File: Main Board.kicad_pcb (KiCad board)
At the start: 2 copper layers, 371 parts, among them J1 Motor Y, J10 CA58SUB-B, J11 PC6 EPSON MAINBOARD, J12 Y AXIS, J13 Z AXIS, J14 LED 1, J15 LED 2, J16 Power Input, J17 VS, J18 12V, J19 5V, J2 Motor Z, J20 3.3V, J21 TABLE SENSOR, J22 INPUT1, J23 INPUT2, J24 PHOTO SENSOR EMITER, J25 PHOTO SENSOR RECEIVER, J26 ANALOG, J27 INPUT3, J28 OUT1, J29 OUT2, J3 USB_B, J30 RELAY, J31 EMERGENCY, J32 EPSON POWER IN, J33 EPSON BOARD POWER, J34 Display, J35 SPI Interface, J36 I2C Interface, J37 LED4, J38 LED3, J39 Key 3, J4 SWD, J40 Key 4, J41 Key 1, J42 Key 2, J5 DEBUG, J6 LIMIT Y BACK, J7 LIMIT Y FRONT, J8 LIMIT Z UP, J9 LIMIT Z DOWN, K1 S13-24V-2C, Q1 2N7002K, Q10 2N7002K, Q11 BC817, Q12 BC817, Q13 BC817, Q14 2N7002K, Q15 2N7002K, Q16 2N7002K, Q17 BC817, Q18 2N7002K, Q19 2N7002K, Q2 2N7002K, Q20 2N7002K, Q21 2N7002K, Q3 2N7002K, Q4 2N7002K, Q5 2N7002K, Q6 2N7002K, Q7 2N7002K, Q8 YJS9435A, Q9 2N7002K, U1 TMC2209-LA, U10 74HC2G32, U11 74HC245, U12 SHTC3, U2 TMC2209-LA, U3 STM32F401VETx, U4 USBUF02W6, U5 74HC245, U6 MCP16301, U7 A4403, U8 MCP16301, U9 MCP6002-xSN, Y1 8MHz

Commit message: Routing of the power supplies are finished
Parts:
- removed the D11 at (93.3, -11.9)
- removed D46, D47, D48: SKL32, Diode_SMD:D_SOD-123F
- removed D49, D50: SD05C.TCT, Diode_SMD:D_SOD-323
- removed the FB1 at (46.9, -7.78)
- removed FB10, FB11: 1000@100MHz, Inductor_SMD:L_0805_2012Metric
- removed FB9: 60Ohm@100MHz, Inductor_SMD:L_0805_2012Metric
- removed the J12 at (83.8, -47.5)
- removed the R12 at (116.4, -77.0)
- removed the R16 at (121.7, -57.5)
- removed the TP11 at (65.0, -72.1)
- removed the U2 at (112.9, -24.8)
- added C79: 1nF, Capacitor_SMD:C_0603_1608Metric, F.Cu at (266.3, 26.7)
- added D23: 1N4448WS-7-F, Diode_SMD:D_SOD-323, F.Cu at (92.5, 44.0)
- added H4: MH, MountingHole:MountingHole_3.5mm_Pad_Via, F.Cu at (121.0, 104.0)
- added Q10: 2N7002K, Package_TO_SOT_SMD:SOT-23, F.Cu at (50.5, -53.2)
- added Q7: 2N7002K, Package_TO_SOT_SMD:SOT-23, F.Cu at (103.2, -51.6)
- added R114: 100Ω, Resistor_SMD:R_0603_1608Metric, F.Cu at (165.4, -34.8)
- added R115: 47kΩ, Resistor_SMD:R_0603_1608Metric, F.Cu at (161.2, -33.7)
- added R116: 47kΩ, Resistor_SMD:R_0603_1608Metric, F.Cu at (165.4, -37.3)
- added R97: 20Ω, Resistor_SMD:R_0603_1608Metric, F.Cu at (253.0, 38.0)
- added TP1: Z_OB2, TestPoint:TestPoint_Pad_D1.5mm, F.Cu at (259.1, 66.9)
- D1, D10, D12, D2, D3, D4, D5, D6, D7, D8, D9: value SK25 -> SMAJ26CA; footprint Diode_SMD:D_SMB -> Diode_SMD:D_SMA
- D11: renamed from C79; value 1nF -> SMAJ26CA; footprint Capacitor_SMD:C_0603_1608Metric -> Diode_SMD:D_SMA
- D13, D16: value SK25 -> OF-SMD2012G-1; footprint Diode_SMD:D_SMB -> Diode_SMD:D_0805_2012Metric
- D14, D15: value SK25 -> SD05C.TCT; footprint Diode_SMD:D_SMB -> Diode_SMD:D_SOD-323
- D18, D39: value SD05C.TCT -> SMAJ26CA; footprint Diode_SMD:D_SOD-323 -> Diode_SMD:D_SMA
- D19: value SD05C.TCT -> OF-SMD2012G-1; footprint Diode_SMD:D_SOD-323 -> Diode_SMD:D_0805_2012Metric
- D20: value OF-SMD2012G-1 -> MMSZ5240B-7-F; footprint Diode_SMD:D_0805_2012Metric -> Diode_SMD:D_SOD-123
- D22: value P4SMA30CA -> B140-13-F
- D24: value MMSZ5240B-7-F -> MMSZ5236BS-7-F; footprint Diode_SMD:D_SOD-123 -> Diode_SMD:D_SOD-323
- D25: value OF-SMD2012G-1 -> B140-13-F; footprint Diode_SMD:D_0805_2012Metric -> Diode_SMD:D_SMA
- D26: value B140-13-F -> SK35SMA
- D28: value MMSZ5236BS-7-F -> 1N4448WS-7-F
- D29: value B140-13-F -> 1N4448WS-7-F; footprint Diode_SMD:D_SMA -> Diode_SMD:D_SOD-323
- D30: value SK35SMA -> 1N4448WS-7-F; footprint Diode_SMD:D_SMA -> Diode_SMD:D_SOD-323
- D35, D36: value 1N4448WS-7-F -> SD05C.TCT
- D37: renamed from D23; value OF-SMD2012G-1 -> SD05C.TCT; footprint Diode_SMD:D_0805_2012Metric -> Diode_SMD:D_SOD-323
- D38: value 1N4448WS-7-F -> SMAJ26CA; footprint Diode_SMD:D_SOD-323 -> Diode_SMD:D_SMA
- D40, D41: value SD05C.TCT -> SKL32; footprint Diode_SMD:D_SOD-323 -> Diode_SMD:D_SOD-123F
- D42, D43: value B130-13-F -> SKL32; footprint Diode_SMD:D_SMA -> Diode_SMD:D_SOD-123F
- D44: value B130-13-F -> SD05C.TCT; footprint Diode_SMD:D_SMA -> Diode_SMD:D_SOD-323
- D45: value SKL32 -> SD05C.TCT; footprint Diode_SMD:D_SOD-123F -> Diode_SMD:D_SOD-323
- F2, F3: value SN010-60 -> 0ZCJ0050AF2E
- F4: value SR050 -> 0ZCK0100FF2E
- FB1: renamed from D37; value 1N4448WS-7-F -> 60Ohm@100MHz; footprint Diode_SMD:D_SOD-323 -> Inductor_SMD:L_0805_2012Metric
- J12: renamed from H4; value MH -> Y AXIS; footprint MountingHole:MountingHole_3.5mm_Pad_Via -> Connector_JST:JST_PH_B3B-PH-K_1x03_P2.00mm_Vertical
- R1: value 1kΩ -> 0Ω
- R10: value 10kΩ -> 47Ω
- R100, R101, R17: value 4.7kΩ -> 330Ω
- R103, R104, R105: value 1kΩ -> 4.7kΩ
- R107, R109: value 2.2kΩ -> 1kΩ
- R108, R31: value 0Ω -> 1kΩ
- R110: value 100Ω -> 2.2kΩ
- R111: value 100Ω -> 0Ω
- R112: value 47kΩ -> 2.2kΩ
- R113, R23, R24, R25: value 47kΩ -> 100Ω
- R12: renamed from Q7; value 2N7002K -> 10kΩ; footprint Package_TO_SOT_SMD:SOT-23 -> Resistor_SMD:R_0603_1608Metric
- R13: value 330Ω -> 0Ω
- R15: value 4.7kΩ -> 0Ω
- R16: renamed from Q10; value 2N7002K -> 0Ω; footprint Package_TO_SOT_SMD:SOT-23 -> Resistor_SMD:R_0603_1608Metric
- R19, R20, R21, R62: value 100Ω -> 4.7kΩ
- R2, R6: value 100kΩ -> 1kΩ
- R27, R84: value 100Ω -> 47kΩ
- R28, R40: value 1kΩ -> 47kΩ
- R29: value 0Ω -> 47kΩ
- R3, R7: value 100mΩ -> 100kΩ; footprint Resistor_SMD:R_2010_5025Metric -> Resistor_SMD:R_0603_1608Metric
- R30: value 0Ω -> 100Ω
- R32: value NI -> 0Ω
- R35: value 100Ω -> NI
- R36: value 100kΩ -> 0Ω
- R37: value 47kΩ -> 0Ω
- R39: value 1kΩ -> 100kΩ
- R41: value 1kΩ -> 100Ω
- R42: value 10kΩ -> 1kΩ; footprint Resistor_SMD:R_0805_2012Metric -> Resistor_SMD:R_0603_1608Metric
- R43: value 330Ω -> 1kΩ
- R45: value 100kΩ -> 10kΩ; footprint Resistor_SMD:R_0603_1608Metric -> Resistor_SMD:R_0805_2012Metric
- R46: value 2.7kΩ -> 330Ω
- R47: value 140kΩ -> 1kΩ
- R48: value 10kΩ -> 100kΩ
- R49: value 100kΩ -> 2.7kΩ
- R5: value 1kΩ -> 100mΩ; footprint Resistor_SMD:R_0603_1608Metric -> Resistor_SMD:R_2010_5025Metric
- R50: value 47Ω -> 140kΩ
- R51: value 100mΩ -> 10kΩ; footprint Resistor_SMD:R_1206_3216Metric -> Resistor_SMD:R_0603_1608Metric
- R52: value 100mΩ -> 100kΩ; footprint Resistor_SMD:R_1206_3216Metric -> Resistor_SMD:R_0603_1608Metric
- R53: value 31.2kΩ -> 47Ω
- R54: value 10kΩ -> 100mΩ; footprint Resistor_SMD:R_0603_1608Metric -> Resistor_SMD:R_1206_3216Metric
- R55: value 3.92kΩ -> 100mΩ; footprint Resistor_SMD:R_0603_1608Metric -> Resistor_SMD:R_1206_3216Metric
- R56: value 750Ω -> 31.2kΩ
- R58: value 4.7kΩ -> 3.92kΩ
- R59: value 4.7kΩ -> 750Ω
- R61: value 100kΩ -> 4.7kΩ
- R63: value 100Ω -> 10kΩ
- R65, R66: value 100kΩ -> 100Ω
- R67, R68, R69: value 47kΩ -> 100kΩ
- R71, R72, R73: value NI -> 47kΩ
- R77: value 10kΩ -> NI
- R79: value 100kΩ -> NI
- R80: value 100kΩ -> 10kΩ
- R81: value 47kΩ -> NI
- R82, R83, R95: value 100Ω -> 100kΩ
- R85: value 0Ω -> 100Ω; footprint Resistor_SMD:R_0805_2012Metric -> Resistor_SMD:R_0603_1608Metric
- R86, R87: value NI -> 100Ω; footprint Resistor_SMD:R_0805_2012Metric -> Resistor_SMD:R_0603_1608Metric
- R88: value 100kΩ -> 0Ω; footprint Resistor_SMD:R_0603_1608Metric -> Resistor_SMD:R_0805_2012Metric
- R89: value 100kΩ -> NI; footprint Resistor_SMD:R_0603_1608Metric -> Resistor_SMD:R_0805_2012Metric
- R9: value 47RΩ -> 100mΩ; footprint Resistor_SMD:R_0603_1608Metric -> Resistor_SMD:R_2010_5025Metric
- R90: value 1kΩ -> NI; footprint Resistor_SMD:R_0603_1608Metric -> Resistor_SMD:R_0805_2012Metric
- R93: value 20Ω -> 1kΩ
- R94: value 20Ω -> 100kΩ
- R96: value 100Ω -> 20Ω
- R98: value 330Ω -> 100Ω
- R99: value 4.7kΩ -> 100Ω
- TP11: renamed from R97; value 330Ω -> 3.3V; footprint Resistor_SMD:R_0603_1608Metric -> TestPoint:TestPoint_Pad_D1.5mm
- U2: renamed from TP1; value Z_OB2 -> TMC2209-LA; footprint TestPoint:TestPoint_Pad_D1.5mm -> footprints:TMC2209-LA
- moved R3 224.9 mm to (253.9, 69.4)
- moved FB3 224.4 mm to (255.1, 64.1)
- moved FB2 223.7 mm to (263.0, 53.9)
- moved D3 223.4 mm to (249.5, 54.7)
- moved C9 222.4 mm to (263.3, 59.2)
- moved C6 221.9 mm to (262.8, 56.6)
- moved FB1 219.6 mm to (241.3, 71.8)
- moved D2 218.1 mm to (241.5, 59.3)
- moved FB4 217.4 mm to (245.7, 70.2)
- moved C4 216.9 mm to (259.3, 61.0)
- moved C1 216.7 mm to (226.5, 66.0)
- moved J1 216.7 mm to (226.5, 55.8)
- moved U1 216.5 mm to (257.2, 56.1)
- moved D1 216.3 mm to (227.0, 74.1)
- moved D5 215.4 mm to (241.5, 54.7)
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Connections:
- D1 pad 1: VS -> Net-(C12-Pad1)
- D1 pad 2: Net-(C12-Pad1) -> GND
- D10 pad 1: Net-(C26-Pad1) -> Net-(C25-Pad2)
- D11 pad 1: KEY_3 -> Net-(C27-Pad2)
- D11 pad 2: GND -> Net-(C25-Pad2)
- D12 pad 1: Net-(C28-Pad1) -> Net-(C26-Pad1)
- D12 pad 2: GND -> Net-(C28-Pad1)
- D13 pad 1: VS -> /Microcontroller/LED_STATUS
- D13 pad 2: Net-(C27-Pad2) -> Net-(D13-Pad2)
- D14 pad 1: Net-(C27-Pad2) -> /Sockets/OPE
- D15 pad 1: VS -> /Sockets/OPC1
- D15 pad 2: Net-(C25-Pad2) -> GND
- D16 pad 1: Net-(C25-Pad2) -> GND
- D16 pad 2: GND -> Net-(D16-Pad2)
- D17 pad 1: /Microcontroller/LED_STATUS -> GND
- D18 pad 1: /Sockets/OPE -> GND
- D18 pad 2: GND -> Net-(D18-Pad2)
- D19 pad 1: /Sockets/OPC1 -> GND
- D19 pad 2: GND -> Net-(D19-Pad2)
- D2 pad 1: Net-(C12-Pad1) -> Net-(C14-Pad1)
- D20 pad 1: GND -> VS
- D22 pad 1: GND -> Net-(C51-Pad2)
- D22 pad 2: Net-(D22-Pad2) -> GND
- D24 pad 1: VS -> +12V
- D24 pad 2: Net-(D24-Pad2) -> Net-(D23-Pad2)
- D25 pad 1: GND -> Net-(C61-Pad2)
- D25 pad 2: Net-(D25-Pad2) -> GND
- D26 pad 1: Net-(C51-Pad2) -> Net-(C59-Pad2)
- D26 pad 2: GND -> Net-(D26-Pad2)
- D27 pad 1: Net-(C51-Pad1) -> Net-(C61-Pad1)
- D27 pad 2: Net-(D27-Pad2) -> +3V3
- D28 pad 1: +12V -> Net-(D28-Pad1)
- D28 pad 2: Net-(D27-Pad2) -> GND
- D29 pad 1: Net-(C61-Pad2) -> Net-(D29-Pad1)
- D3 pad 1: VS -> Net-(C13-Pad2)
- D3 pad 2: Net-(C14-Pad1) -> GND
- D30 pad 1: Net-(C59-Pad2) -> VDDA
- D30 pad 2: Net-(D30-Pad2) -> Net-(C73-Pad1)
- D31 pad 1: Net-(C61-Pad1) -> Net-(C73-Pad1)
- D31 pad 2: +3V3 -> GND
- D32 pad 1: Net-(D32-Pad1) -> VDDA
- D32 pad 2: GND -> Net-(C74-Pad1)
- D33 pad 1: Net-(D33-Pad1) -> Net-(C74-Pad1)
- D34 pad 1: VDDA -> Net-(D34-Pad1)
- D34 pad 2: Net-(C73-Pad1) -> GND
- D35 pad 1: Net-(C73-Pad1) -> Net-(D35-Pad1)
- D36 pad 1: VDDA -> Net-(D36-Pad1)
- D36 pad 2: Net-(C74-Pad1) -> GND
- D37 pad 1: GND -> Net-(D37-Pad1)
- D37 pad 2: Net-(D23-Pad2) -> GND
- D38 pad 1: Net-(D38-Pad1) -> 12V_PROTECTED
- D39 pad 1: Net-(D39-Pad1) -> GND
- D39 pad 2: GND -> Net-(D39-Pad2)
- D4 pad 1: Net-(C14-Pad1) -> Net-(C11-Pad2)
- D40 pad 1: Net-(D40-Pad1) -> +3V3
- D40 pad 2: GND -> I2C_SCL
- D41 pad 1: Net-(D41-Pad1) -> I2C_SCL
- D42 pad 1: 12V_PROTECTED -> +3V3
- D42 pad 2: GND -> I2C_SDA
- D43 pad 1: Net-(D43-Pad1) -> I2C_SDA
- D44 pad 1: VS -> Net-(D44-Pad1)
- D44 pad 2: Net-(D43-Pad1) -> GND
- D45 pad 1: +3V3 -> Net-(D45-Pad1)
- D45 pad 2: I2C_SCL -> GND
- D5 pad 1: VS -> Net-(C13-Pad2)
- D5 pad 2: Net-(C13-Pad2) -> Net-(C11-Pad2)
- D6 pad 1: Net-(C13-Pad2) -> Net-(C12-Pad1)
- D6 pad 2: GND -> Net-(C14-Pad1)
- D7 pad 1: VS -> Net-(C26-Pad1)
- D7 pad 2: Net-(C11-Pad2) -> GND
- D8 pad 1: Net-(C11-Pad2) -> Net-(C28-Pad1)
- D9 pad 1: VS -> Net-(C27-Pad2)
- D9 pad 2: Net-(C26-Pad1) -> GND
- F1 pad 1: Net-(D22-Pad2) -> Net-(D18-Pad2)
- FB1 pad 1: Net-(C74-Pad1) -> Net-(C11-Pad2)
- FB1 pad 2: GND -> Net-(FB1-Pad2)
- FB2 pad 1: Net-(C11-Pad2) -> Net-(C13-Pad2)
- FB3 pad 1: Net-(C13-Pad2) -> Net-(C14-Pad1)
- FB4 pad 1: Net-(C14-Pad1) -> Net-(C12-Pad1)
- FB5 pad 1: Net-(C12-Pad1) -> Net-(C25-Pad2)
- FB6 pad 1: Net-(C25-Pad2) -> Net-(C27-Pad2)
- FB7 pad 1: Net-(C27-Pad2) -> Net-(C28-Pad1)
- FB8 pad 1: Net-(C28-Pad1) -> Net-(C26-Pad1)
- J12 pad 1: Net-(H4-Pad1) -> /Sockets/YSTEP
- J28 pad 2: Net-(D39-Pad1) -> Net-(D35-Pad1)
- J29 pad 2: Net-(D40-Pad1) -> Net-(D36-Pad1)
- J30 pad 1: Net-(D41-Pad1) -> Net-(D37-Pad1)
- J31 pad 2: Net-(D43-Pad1) -> Net-(D39-Pad2)
- J37 pad 2: Net-(D49-Pad1) -> Net-(D44-Pad1)
- J38 pad 2: Net-(D50-Pad1) -> Net-(D45-Pad1)
- K1 pad 1: Net-(D43-Pad1) -> Net-(D39-Pad2)
- Q11 pad 1: Net-(D32-Pad1) -> Net-(D28-Pad1)
- Q12 pad 1: Net-(D33-Pad1) -> Net-(D29-Pad1)
- Q13 pad 1: Net-(D38-Pad1) -> Net-(D34-Pad1)
- Q14 pad 3: Net-(D39-Pad1) -> Net-(D35-Pad1)
- Q15 pad 3: Net-(D40-Pad1) -> Net-(D36-Pad1)
- Q16 pad 3: Net-(D41-Pad1) -> Net-(D37-Pad1)
- Q18 pad 3: Net-(D50-Pad1) -> Net-(D45-Pad1)
- Q19 pad 3: Net-(D49-Pad1) -> Net-(D44-Pad1)
- Q8 pad 4: Net-(D24-Pad2) -> Net-(D20-Pad2)
- Q8 pad 5: Net-(D22-Pad2) -> Net-(D18-Pad2)
- Q8 pad 6: Net-(D22-Pad2) -> Net-(D18-Pad2)
- Q8 pad 7: Net-(D22-Pad2) -> Net-(D18-Pad2)
- Q8 pad 8: Net-(D22-Pad2) -> Net-(D18-Pad2)
- R1 pad 1: UART_TX -> +3V3
- R1 pad 2: UART_RX -> +3V3
- R10 pad 1: VDD -> VDDA
- R10 pad 2: NRST -> Net-(C31-Pad1)
- R100 pad 1: Net-(J40-Pad1) -> Net-(J38-Pad1)
- R101 pad 1: Net-(J41-Pad1) -> Net-(J37-Pad1)
- R102 pad 1: Net-(J42-Pad1) -> Net-(J39-Pad1)
- R103 pad 1: KEY_3 -> Net-(J40-Pad1)
- R103 pad 2: Net-(J39-Pad1) -> +5V
- R104 pad 1: KEY_4 -> Net-(J41-Pad1)
- R104 pad 2: Net-(J40-Pad1) -> +5V
- R105 pad 1: KEY_1 -> Net-(J42-Pad1)
- R105 pad 2: Net-(J41-Pad1) -> +5V
- R106 pad 1: KEY_2 -> KEY_3
- R106 pad 2: Net-(J42-Pad1) -> Net-(J39-Pad1)
- R107 pad 1: +3V3 -> KEY_4
- R107 pad 2: I2C_SDA -> Net-(J40-Pad1)
- R108 pad 1: I2C_SDA -> KEY_1
- R108 pad 2: Net-(R108-Pad2) -> Net-(J41-Pad1)
- R109 pad 1: +3V3 -> KEY_2
- R109 pad 2: I2C_SCL -> Net-(J42-Pad1)
- R11 pad 1: Net-(R11-Pad1) -> VDD
- R11 pad 2: GND -> NRST
- R110 pad 1: +5V -> +3V3
- R110 pad 2: Net-(Q20-Pad1) -> I2C_SDA
- R111 pad 1: +12V -> I2C_SDA
- R111 pad 2: Net-(Q21-Pad1) -> Net-(R111-Pad2)
- R112 pad 1: 5V_DETECT -> +3V3
- R112 pad 2: +3V3 -> I2C_SCL
- R113 pad 1: 12V_DETECT -> +5V
- R113 pad 2: +3V3 -> Net-(Q20-Pad1)
- R12 pad 1: Net-(Q7-Pad1) -> Net-(R12-Pad1)
- R13 pad 1: Net-(J4-Pad1) -> Net-(R13-Pad1)
- R13 pad 2: VDD -> GND
- R14 pad 1: +3V3 -> Net-(J4-Pad1)
- R14 pad 2: Net-(D17-Pad2) -> VDD
- R15 pad 1: Net-(J6-Pad1) -> VDDA
- R16 pad 1: Net-(Q10-Pad1) -> VDD
- R16 pad 2: GND -> +3V3
- R17 pad 1: Net-(J8-Pad1) -> +3V3
- R17 pad 2: +3V3 -> Net-(D13-Pad2)
- R18 pad 1: Net-(J9-Pad1) -> Net-(J6-Pad1)
- R19 pad 1: Net-(J6-Pad1) -> Net-(J7-Pad1)
- R19 pad 2: Net-(Q1-Pad1) -> +3V3
- R2 pad 1: GND -> UART_TX
- R2 pad 2: Y_ENN -> UART_RX
- R20 pad 1: Net-(J7-Pad1) -> Net-(J8-Pad1)
- R20 pad 2: Net-(Q2-Pad1) -> +3V3
- R21 pad 1: Net-(J8-Pad1) -> Net-(J9-Pad1)
- R21 pad 2: Net-(Q3-Pad1) -> +3V3
- R22 pad 1: Net-(J9-Pad1) -> Net-(J6-Pad1)
- R22 pad 2: Net-(Q4-Pad1) -> Net-(Q1-Pad1)
- R23 pad 1: LIMIT_Y_BACK -> Net-(J7-Pad1)
- R23 pad 2: +3V3 -> Net-(Q2-Pad1)
- R24 pad 1: LIMIT_Y_FRONT -> Net-(J8-Pad1)
- R24 pad 2: +3V3 -> Net-(Q3-Pad1)
- R25 pad 1: LIMIT_Z_UP -> Net-(J9-Pad1)
- R25 pad 2: +3V3 -> Net-(Q4-Pad1)
- R26 pad 1: LIMIT_Z_DOWN -> LIMIT_Y_BACK
- R27 pad 1: PE_SIGNAL -> LIMIT_Y_FRONT
- R27 pad 2: Net-(Q5-Pad1) -> +3V3
- R28 pad 1: /Sockets/OPE -> LIMIT_Z_UP
- R28 pad 2: /Sockets/PE_S -> +3V3
- R29 pad 1: /Sockets/PC1 -> LIMIT_Z_DOWN
- R29 pad 2: /Sockets/OPC1 -> +3V3
- R3 pad 1: Net-(C8-Pad1) -> GND
- R3 pad 2: GND -> Y_ENN
- R30 pad 1: /Sockets/PF_B -> PE_SIGNAL
- R30 pad 2: /Sockets/OPF_B -> Net-(Q5-Pad1)
- R31 pad 1: /Sockets/PF_A -> /Sockets/OPE
- R31 pad 2: /Sockets/OPF_A -> /Sockets/PE_S
- R32 pad 1: /Sockets/PE -> /Sockets/PC1
- R32 pad 2: /Sockets/OPE -> /Sockets/OPC1
- R33 pad 1: /Sockets/APG -> /Sockets/PF_B
- R33 pad 2: /Sockets/OAPG -> /Sockets/OPF_B
- R34 pad 1: /Sockets/APGHP -> /Sockets/PF_A
- R34 pad 2: /Sockets/OAPGHP -> /Sockets/OPF_A
- R35 pad 1: /Sockets/3.3V -> /Sockets/PE
- R35 pad 2: Net-(Q6-Pad1) -> /Sockets/OPE
- R36 pad 1: Net-(Q6-Pad1) -> /Sockets/APG
- R36 pad 2: GND -> /Sockets/OAPG
- R37 pad 1: PRINTER_POWER_DETECT -> /Sockets/APGHP
- R37 pad 2: +3V3 -> /Sockets/OAPGHP
- R38 pad 1: PC1_SIGNAL -> /Sockets/3.3V
- R38 pad 2: Net-(Q7-Pad1) -> Net-(Q6-Pad1)
- R39 pad 1: ENC1_B -> Net-(Q6-Pad1)
- R39 pad 2: /Sockets/PF_B -> GND
- R4 pad 1: Net-(C10-Pad1) -> Net-(C8-Pad1)
- R40 pad 1: ENC1_A -> PRINTER_POWER_DETECT
- R40 pad 2: /Sockets/PF_A -> +3V3
- R41 pad 1: /Sockets/OPC1 -> PC1_SIGNAL
- R41 pad 2: /Sockets/3.3V -> Net-(Q7-Pad1)
- R42 pad 1: VS -> ENC1_B
- R42 pad 2: Net-(D20-Pad2) -> /Sockets/PF_B
- R43 pad 1: +3V3 -> ENC1_A
- R43 pad 2: Net-(D21-Pad2) -> /Sockets/PF_A
- R44 pad 1: +5V -> /Sockets/OPC1
- R44 pad 2: Net-(D23-Pad2) -> /Sockets/3.3V
- R45 pad 1: Net-(D24-Pad2) -> VS
- R45 pad 2: GND -> Net-(D16-Pad2)
- R46 pad 1: +12V -> +3V3
- R46 pad 2: Net-(D25-Pad2) -> Net-(D17-Pad2)
- R47 pad 1: +12V -> +5V
- R47 pad 2: Net-(R47-Pad2) -> Net-(D19-Pad2)
- R48 pad 1: Net-(R47-Pad2) -> Net-(D20-Pad2)
- R49 pad 1: Net-(R49-Pad1) -> +12V
- R49 pad 2: VS -> Net-(D21-Pad2)
- R5 pad 1: UART_TX -> Net-(C10-Pad1)
- R5 pad 2: UART_RX -> GND
- R50 pad 1: Net-(D30-Pad2) -> +12V
- R50 pad 2: Net-(C60-Pad1) -> Net-(R50-Pad2)
- R51 pad 1: Net-(D30-Pad2) -> Net-(R50-Pad2)
- R52 pad 1: GND -> Net-(R52-Pad1)
- R52 pad 2: Net-(D30-Pad2) -> VS
- R53 pad 1: +3V3 -> Net-(D26-Pad2)
- R53 pad 2: Net-(R53-Pad2) -> Net-(C60-Pad1)
- R54 pad 1: Net-(R53-Pad2) -> Net-(D26-Pad2)
- R55 pad 1: Net-(C66-Pad2) -> GND
- R55 pad 2: +5V -> Net-(D26-Pad2)
- R56 pad 1: GND -> +3V3
- R56 pad 2: Net-(C66-Pad2) -> Net-(R56-Pad2)
- R57 pad 1: 24V_PROTECTED -> Net-(R56-Pad2)
- R57 pad 2: Net-(J21-Pad2) -> GND
- R58 pad 1: Net-(J22-Pad1) -> Net-(C66-Pad2)
- R58 pad 2: +3V3 -> +5V
- R59 pad 1: Net-(J23-Pad1) -> GND
- R59 pad 2: +3V3 -> Net-(C66-Pad2)
- R6 pad 1: GND -> UART_TX
- R6 pad 2: Z_ENN -> UART_RX
- R60 pad 2: Net-(J25-Pad2) -> Net-(J21-Pad2)
- R61 pad 1: Net-(D32-Pad1) -> Net-(J22-Pad1)
- R61 pad 2: Net-(J21-Pad2) -> +3V3
- R62 pad 1: Net-(J22-Pad1) -> Net-(J23-Pad1)
- R62 pad 2: Net-(Q9-Pad1) -> +3V3
- R63 pad 1: Net-(J23-Pad1) -> 24V_PROTECTED
- R63 pad 2: Net-(Q10-Pad1) -> Net-(J25-Pad2)
- R64 pad 1: Net-(D32-Pad1) -> Net-(D28-Pad1)
- R64 pad 2: GND -> Net-(J21-Pad2)
- R65 pad 1: Net-(D33-Pad1) -> Net-(J22-Pad1)
- R65 pad 2: Net-(J25-Pad2) -> Net-(Q9-Pad1)
- R66 pad 1: Net-(D33-Pad1) -> Net-(J23-Pad1)
- R66 pad 2: GND -> Net-(Q10-Pad1)
- R67 pad 1: INPUT1 -> Net-(D28-Pad1)
- R67 pad 2: +3V3 -> GND
- R68 pad 1: INPUT2 -> Net-(D29-Pad1)
- R68 pad 2: +3V3 -> Net-(J25-Pad2)
- R69 pad 1: +3V3 -> Net-(D29-Pad1)
- R69 pad 2: TABLE_SENSOR -> GND
- R7 pad 1: Net-(C22-Pad1) -> GND
- R7 pad 2: GND -> Z_ENN
- R70 pad 1: +3V3 -> INPUT1
- R70 pad 2: PHOTO_SENSOR -> +3V3
- R71 pad 1: Net-(J26-Pad1) -> INPUT2
- R71 pad 2: Net-(C71-Pad1) -> +3V3
- R72 pad 1: Net-(C71-Pad1) -> +3V3
- R72 pad 2: GND -> TABLE_SENSOR
- R73 pad 1: Net-(J26-Pad3) -> +3V3
- R73 pad 2: Net-(C72-Pad1) -> PHOTO_SENSOR
- R74 pad 1: Net-(C72-Pad1) -> Net-(J26-Pad1)
- R74 pad 2: GND -> Net-(C71-Pad1)
- R75 pad 1: Net-(C73-Pad1) -> Net-(C71-Pad1)
- R75 pad 2: Net-(C71-Pad1) -> GND
- R76 pad 1: Net-(C74-Pad1) -> Net-(J26-Pad3)
- R77 pad 1: 24V_PROTECTED -> Net-(C72-Pad1)
- R77 pad 2: Net-(J27-Pad2) -> GND
- R78 pad 1: Net-(J27-Pad2) -> Net-(C73-Pad1)
- R78 pad 2: GND -> Net-(C71-Pad1)
- R79 pad 1: Net-(D38-Pad1) -> Net-(C74-Pad1)
- R79 pad 2: Net-(J27-Pad2) -> Net-(C72-Pad1)
- R8 pad 1: Net-(C24-Pad1) -> Net-(C22-Pad1)
- R80 pad 1: Net-(D38-Pad1) -> 24V_PROTECTED
- R80 pad 2: GND -> Net-(J27-Pad2)
- R81 pad 1: +3V3 -> Net-(J27-Pad2)
- R81 pad 2: INPUT3 -> GND
- R82 pad 1: OUTPUT1 -> Net-(D34-Pad1)
- R82 pad 2: Net-(Q14-Pad1) -> Net-(J27-Pad2)
- R83 pad 1: OUTPUT2 -> Net-(D34-Pad1)
- R83 pad 2: Net-(Q15-Pad1) -> GND
- R84 pad 1: RELAY -> +3V3
- R84 pad 2: Net-(Q16-Pad1) -> INPUT3
- R85 pad 1: Net-(K1-Pad13) -> OUTPUT1
- R85 pad 2: Net-(C76-Pad1) -> Net-(Q14-Pad1)
- R86 pad 1: Net-(K1-Pad6) -> OUTPUT2
- R86 pad 2: Net-(K1-Pad11) -> Net-(Q15-Pad1)
- R87 pad 1: Net-(K1-Pad11) -> RELAY
- R87 pad 2: Net-(C76-Pad2) -> Net-(Q16-Pad1)
- R88 pad 1: Net-(Q17-Pad1) -> Net-(K1-Pad13)
- R88 pad 2: Net-(D43-Pad1) -> Net-(C76-Pad1)
- R89 pad 1: Net-(Q17-Pad1) -> Net-(K1-Pad6)
- R89 pad 2: GND -> Net-(K1-Pad11)
- R9 pad 1: VDDA -> Net-(C24-Pad1)
- R9 pad 2: Net-(C31-Pad1) -> GND
- R90 pad 1: +3V3 -> Net-(K1-Pad11)
- R90 pad 2: EMERGENCY -> Net-(C76-Pad2)
- R91 pad 1: +3V3 -> Net-(Q17-Pad1)
- R91 pad 2: Y_ENABLE -> Net-(D39-Pad2)
- R92 pad 1: +3V3 -> Net-(Q17-Pad1)
- R92 pad 2: Z_ENABLE -> GND
- R93 pad 1: Net-(J36-Pad2) -> +3V3
- R93 pad 2: I2C_SDA -> EMERGENCY
- R94 pad 1: Net-(J36-Pad4) -> +3V3
- R94 pad 2: I2C_SCL -> Y_ENABLE
- R95 pad 1: LED3 -> +3V3
- R95 pad 2: Net-(Q18-Pad1) -> Z_ENABLE
- R96 pad 1: LED4 -> Net-(J36-Pad2)
- R96 pad 2: Net-(Q19-Pad1) -> I2C_SDA
- R98 pad 1: Net-(J37-Pad1) -> LED3
- R98 pad 2: +5V -> Net-(Q18-Pad1)
- R99 pad 1: Net-(J39-Pad1) -> LED4
- R99 pad 2: +5V -> Net-(Q19-Pad1)
- TP11 pad 1: Net-(J38-Pad1) -> +3V3
- U1 pad 1: Net-(FB5-Pad2) -> Net-(FB4-Pad2)
- U1 pad 21: Net-(FB3-Pad2) -> Net-(FB2-Pad2)
- U1 pad 24: Net-(FB2-Pad2) -> Net-(FB1-Pad2)
- U1 pad 26: Net-(FB4-Pad2) -> Net-(FB3-Pad2)
- U12 pad 3: Net-(R108-Pad2) -> Net-(R111-Pad2)
- U2 pad 1: Net-(C12-Pad1) -> Net-(FB8-Pad2)
- U3 pad 49: Net-(R12-Pad1) -> Net-(R13-Pad1)
- U3 pad 94: Net-(R11-Pad1) -> Net-(R12-Pad1)
- U6 pad 3: Net-(R47-Pad2) -> Net-(R50-Pad2)
- U7 pad 3: Net-(R49-Pad1) -> Net-(R52-Pad1)
- U8 pad 3: Net-(R53-Pad2) -> Net-(R56-Pad2)
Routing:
- net GND: track 0.00 -> 76.4 mm, vias 0 -> 47
- net +3V3: track 0.00 -> 40.2 mm, vias 0 -> 6
- net +12V: track 0.00 -> 38.1 mm, vias 0 -> 6
- net VS: track 0.00 -> 29.9 mm, vias 0 -> 28
- net Net-(D26-Pad2): track 0.00 -> 16.4 mm, vias 0 -> 2
- net Net-(C66-Pad2): track 0.00 -> 11.3 mm
- net Net-(C61-Pad1): track 0.00 -> 10.4 mm
- net +5V: track 0.00 -> 9.97 mm, vias 0 -> 6
- net Net-(C59-Pad2): track 0.00 -> 9.50 mm
- net Net-(C51-Pad1): track 0.00 -> 9.24 mm
- net Net-(C59-Pad1): track 0.00 -> 8.48 mm, vias 0 -> 2
- net Net-(R56-Pad2): track 0.00 -> 6.43 mm
- net Net-(D20-Pad2): track 0.00 -> 6.15 mm
- net Net-(C56-Pad2): track 0.00 -> 5.80 mm
- net Net-(R50-Pad2): track 0.00 -> 5.49 mm
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- added copper zone on F.Cu, net +12V
- added copper zone on F.Cu, net +3V3
- added copper zone on F.Cu, net +5V
- added copper zone on B.Cu, net GND
- added copper zone on F.Cu, net GND
- added copper zone on F.Cu, net Net-(C51-Pad2)
- added copper zone on F.Cu, net Net-(C59-Pad2)
- added copper zone on F.Cu, net Net-(C61-Pad2)
- added copper zone on F.Cu, net Net-(D18-Pad2)
- added copper zone on F.Cu, net Net-(D26-Pad2)
- added copper zone on F.Cu, net Net-(F1-Pad2)
- added copper zone on F.Cu, net VS
- added copper zone on In1.Cu, net VS
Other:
- board outline added: 156 x 85 mm
- copper layers 2 -> 4
- board text added: "MAX 250x500mm"

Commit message: Rozmieszczenie elementów, trasowanie ścieżek, etap 2/4
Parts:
- added C84: 0.1uF, Capacitor_SMD:C_0603_1608Metric, F.Cu at (90.7, 72.5)
- added FID5: Fiducial, Fiducial:Fiducial_1mm_Mask2mm, F.Cu at (195.0, 33.0)
- added FID6: Fiducial, Fiducial:Fiducial_1mm_Mask2mm, F.Cu at (195.0, 107.0)
- moved J26 193.5 mm to (109.0, 112.0), turned to 180 degrees
- moved J15 193.2 mm to (190.5, 112.0), turned to 180 degrees
- moved R43 190.0 mm to (51.2, 128.5)
- moved J14 187.7 mm to (180.5, 112.0), turned to 180 degrees
- moved Q5 187.6 mm to (103.2, 127.5)
- moved J29 185.1 mm to (185.5, 28.0)
- moved R42 183.1 mm to (51.3, 124.5)
- moved R40 182.9 mm to (67.5, 132.2)
- moved Q7 182.2 mm to (91.2, 130.2)
- moved R30 181.4 mm to (98.5, 129.8)
- moved J30 177.4 mm to (97.0, 112.0), turned to 180 degrees
- moved J27 175.4 mm to (89.0, 112.0), turned to 180 degrees
- moved C48 175.2 mm to (67.5, 129.2)
- moved Q15 175.2 mm to (187.5, 34.0), turned to 90 degrees
- moved R31 174.9 mm to (98.5, 125.8)
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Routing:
- net USB_D-: track 0.00 -> 20.7 mm
- net USB_D+: track 0.00 -> 20.0 mm
- net Net-(C29-Pad1): track 0.00 -> 15.9 mm
- net Net-(C30-Pad1): track 0.00 -> 15.3 mm
- net /Microcontroller/D+: track 0.00 -> 6.07 mm
- net /Microcontroller/D-: track 0.00 -> 3.49 mm
- net VS: track 29.9 -> 31.8 mm, vias 28 -> 29
- net GND: track 76.4 -> 74.9 mm, vias 47 -> 46
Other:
- board size 156 x 85 mm -> 161 x 92 mm
- board text removed: "MAX 250x500mm"

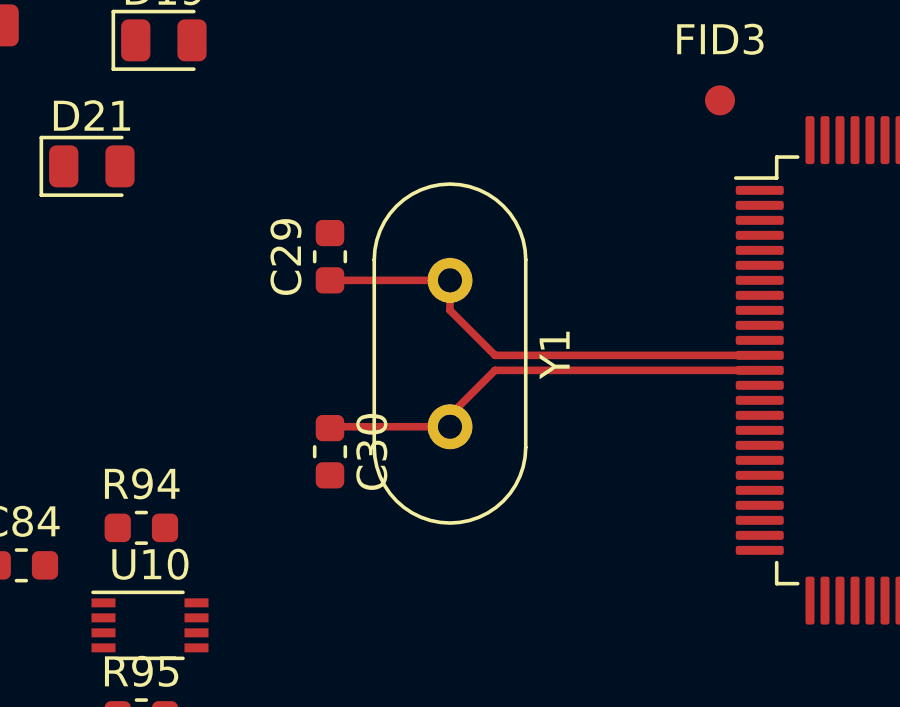
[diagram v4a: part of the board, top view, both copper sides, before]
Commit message: Update Crystal footprint and inductor 3D package on PCB
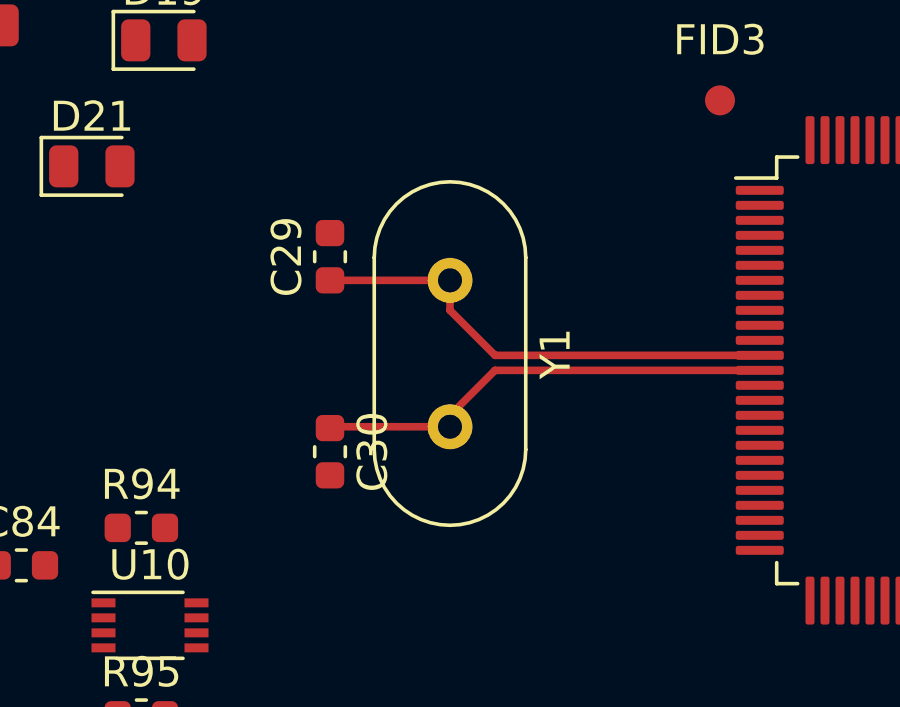
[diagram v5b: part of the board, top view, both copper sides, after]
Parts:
- Y1: footprint Crystal:Crystal_HC49-U_Vertical -> Crystal:Crystal_HC49-4H_Vertical
